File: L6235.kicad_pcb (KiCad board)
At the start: 2 copper layers, 68.6 x 58.4 mm, 28 parts, among them P1 CONN_01X03, U1 L6235N

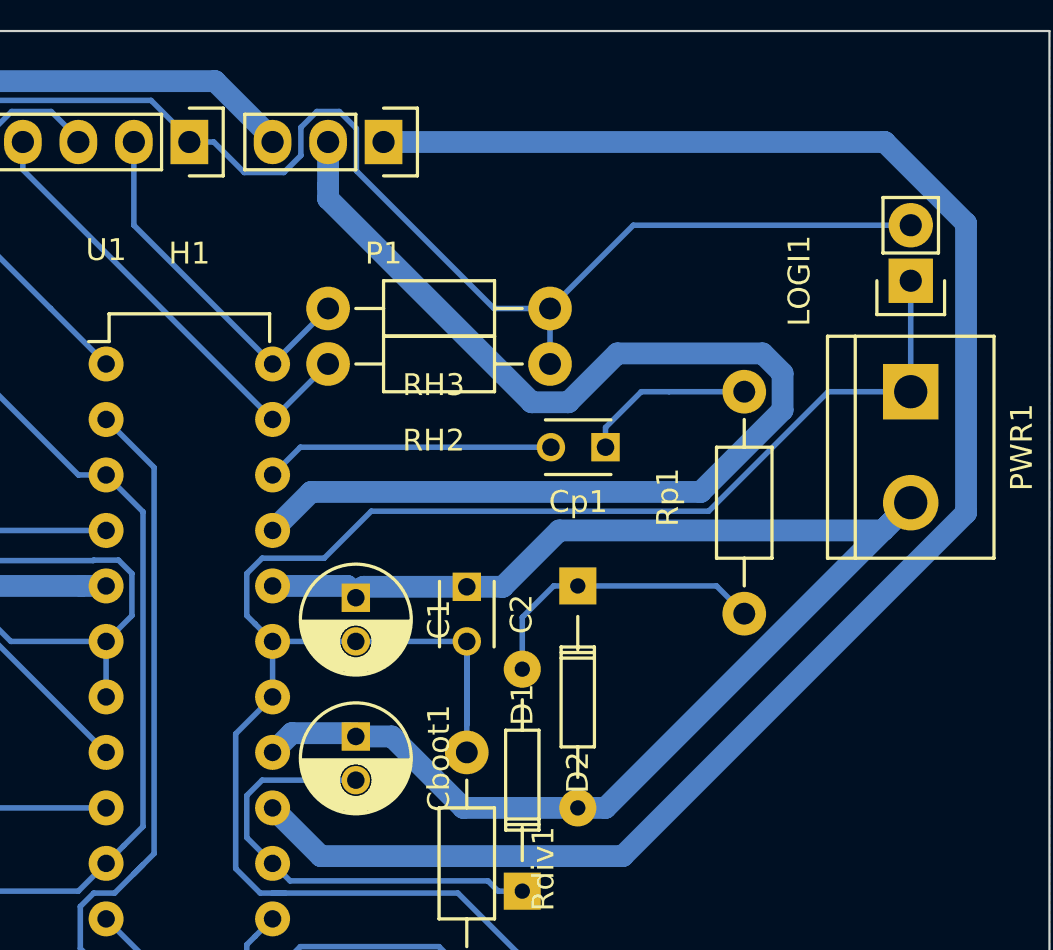
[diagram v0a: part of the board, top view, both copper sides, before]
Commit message: fix: larger GND plan next to Phase2
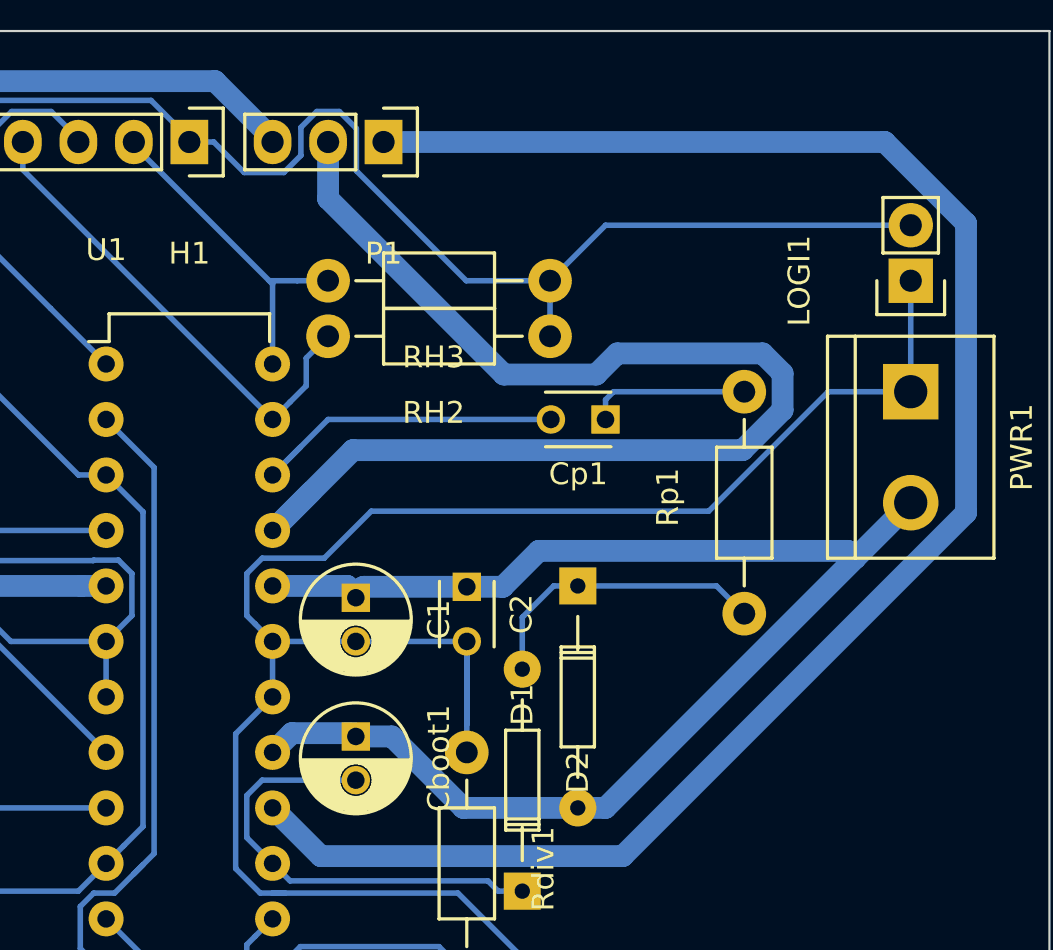
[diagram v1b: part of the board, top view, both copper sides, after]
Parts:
- moved Cp1 1.27 mm to (172.7, 105.4)
- moved RH2 1.27 mm to (170.2, 101.6)
- moved RH3 1.27 mm to (170.2, 99.1)
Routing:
- net VSS: track 67.8 -> 64.5 mm
- net Net-(Cp1-Pad2): track 13.3 -> 15.6 mm
- net /PHASE2: track 55.9 -> 57.3 mm
- net /HALL2: track 21.0 -> 22.3 mm
- net +5V: track 80.6 -> 79.6 mm
- net /HALL3: track 16.4 -> 15.5 mm
- net Net-(Cp1-Pad1): track 7.93 -> 7.41 mm

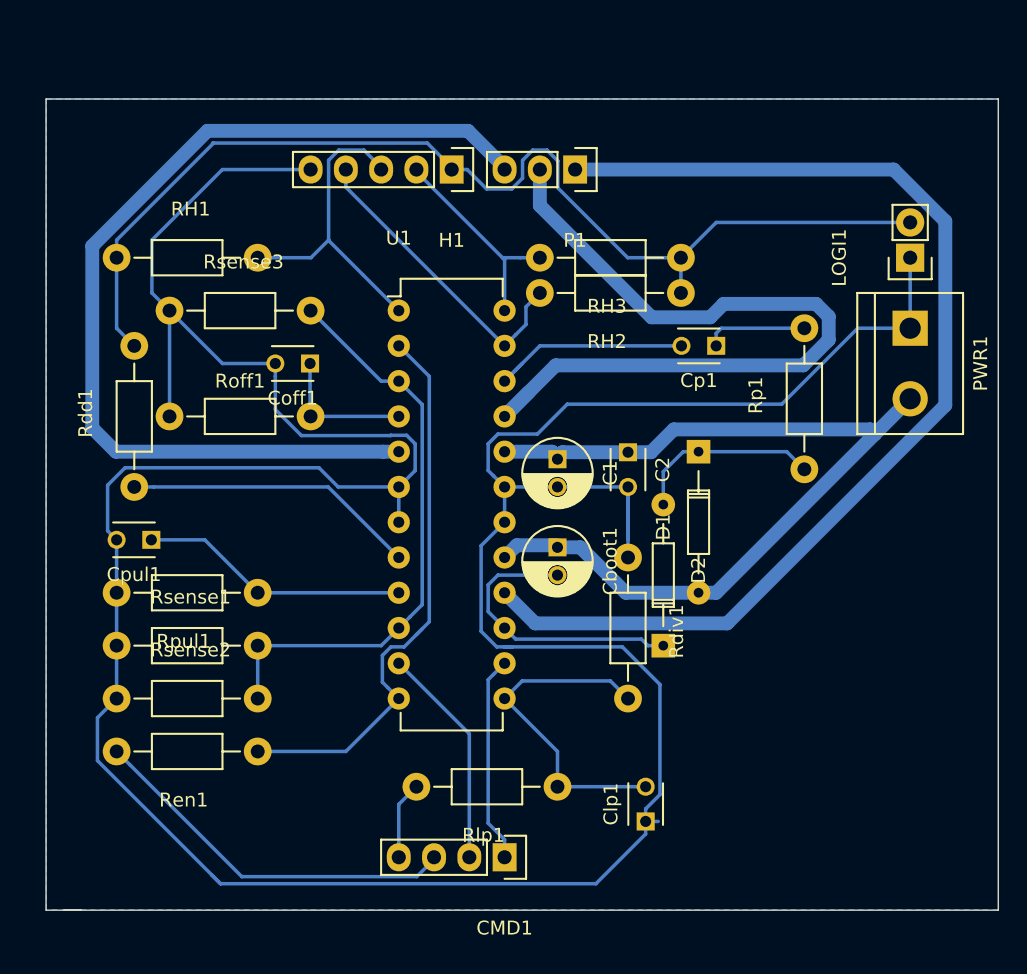
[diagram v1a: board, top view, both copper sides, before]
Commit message: feature: add mounting holes; fix: add GND bridge
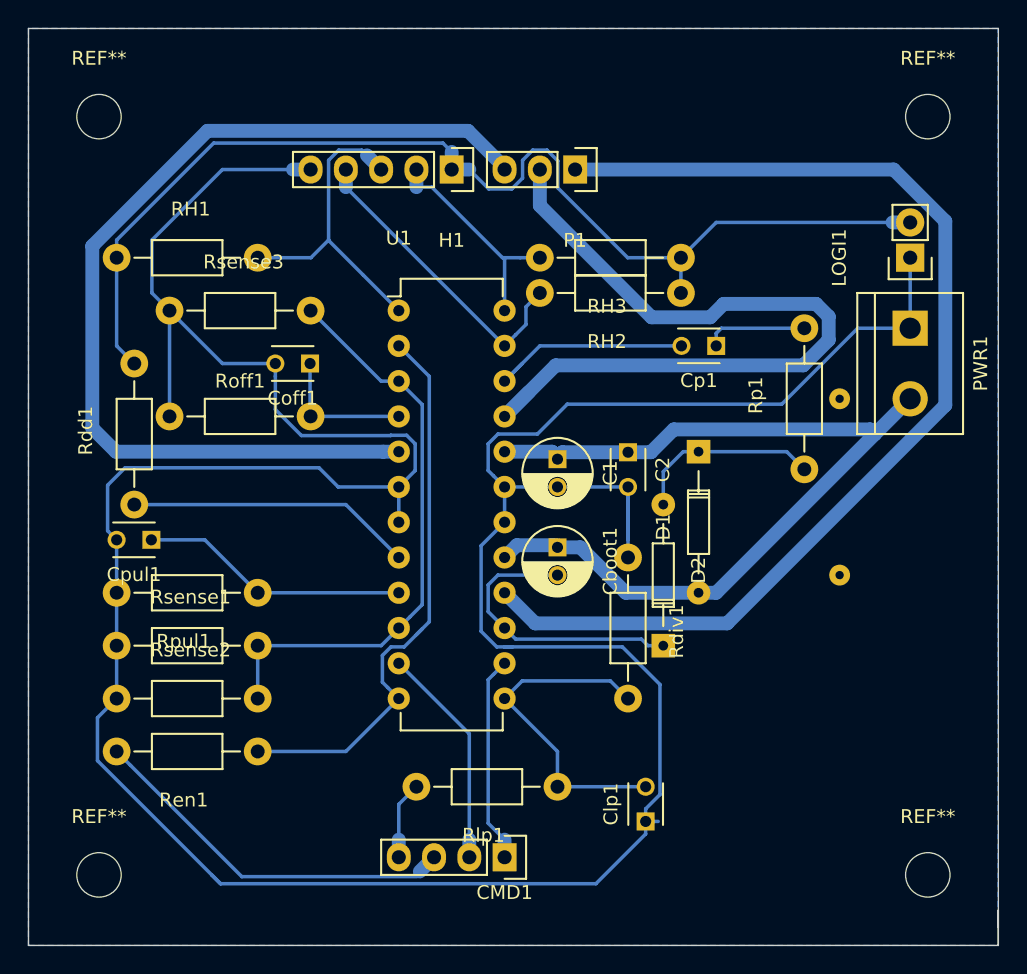
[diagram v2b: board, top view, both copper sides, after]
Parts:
- added ?: , pcb_helpers:pad_gnd, F.Cu at (181.6, 121.9)
- added ?: , pcb_helpers:pad_gnd, F.Cu at (181.6, 109.2)
- added REF**: MountingHole_3.2mm_M3, Mounting_Holes:MountingHole_3.2mm_M3, F.Cu at (188.0, 88.9)
- added REF**: MountingHole_3.2mm_M3, Mounting_Holes:MountingHole_3.2mm_M3, F.Cu at (188.0, 143.5)
- added REF**: MountingHole_3.2mm_M3, Mounting_Holes:MountingHole_3.2mm_M3, F.Cu at (128.3, 88.9)
- added REF**: MountingHole_3.2mm_M3, Mounting_Holes:MountingHole_3.2mm_M3, F.Cu at (128.3, 143.5)
- moved Rdd1 1.27 mm to (130.8, 116.8)
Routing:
- net +5V: track 79.6 -> 81.6 mm
- net /FWD/REV: track 16.1 -> 17.3 mm
- net /HALL3: track 15.5 -> 16.2 mm
- net Net-(Rdd1-Pad1): track 21.2 -> 20.6 mm
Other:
- board size 68.6 x 58.4 mm -> 69.8 x 66 mm
